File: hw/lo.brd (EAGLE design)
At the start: 23.8 x 33 mm, 40 parts, among them U1 ADF4360-9, X1 CLK, X2 DATA, X3 LE, X4 DIVOUT, X7 VIN

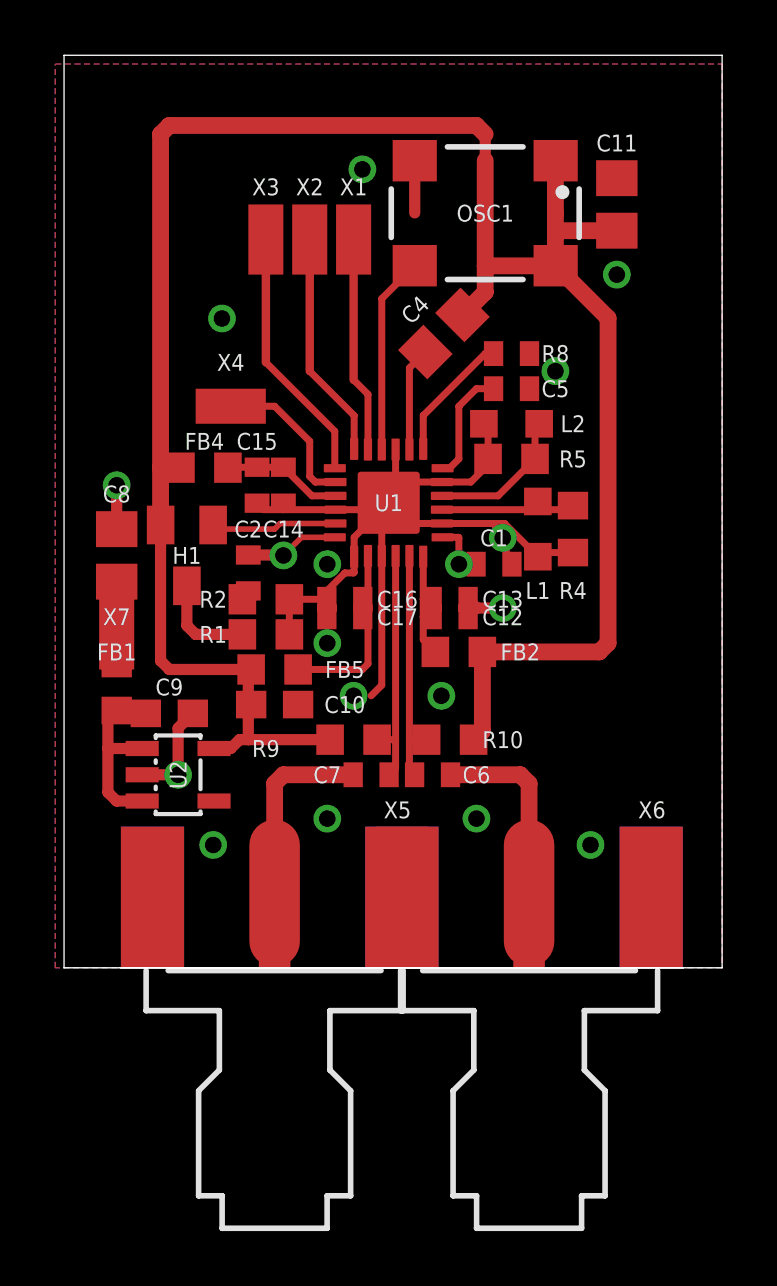
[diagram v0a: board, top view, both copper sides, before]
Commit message: optimize layout for easier soldering
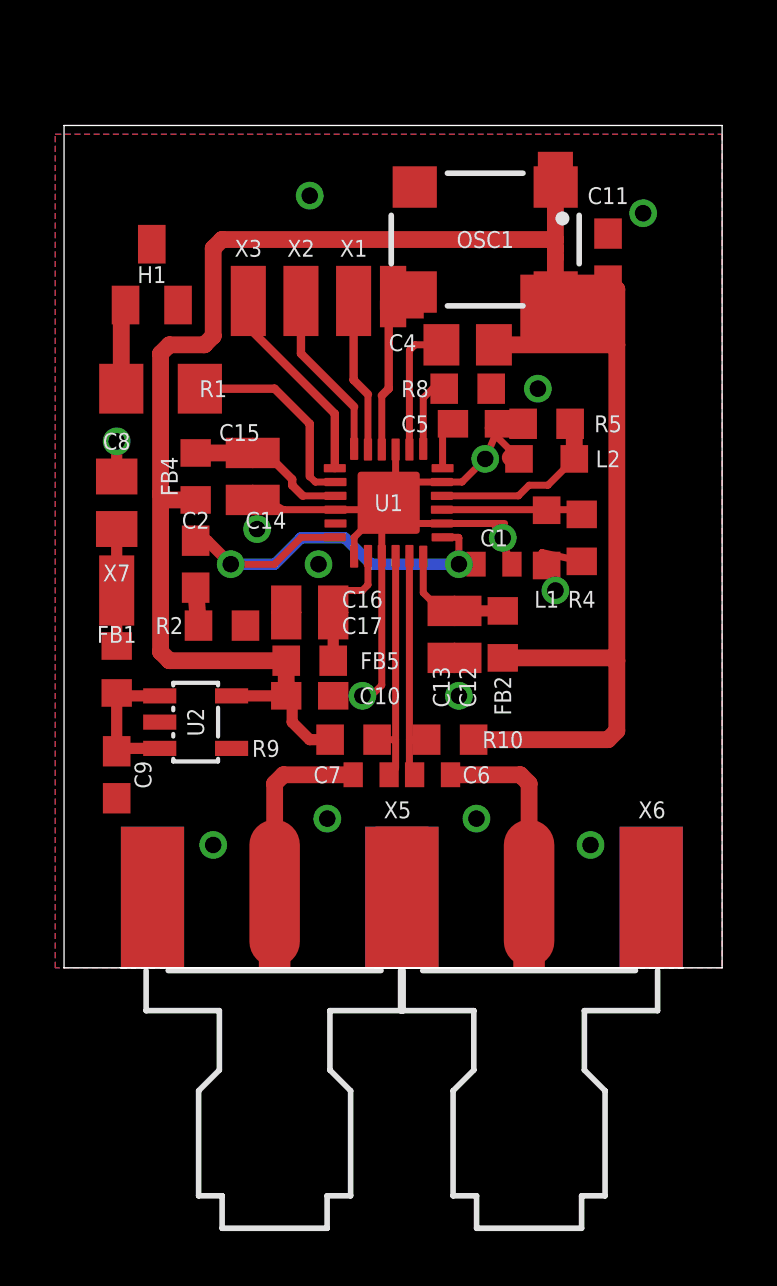
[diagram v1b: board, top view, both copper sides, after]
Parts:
- removed X4: DIVOUT, wirepad:SMD1,27-2,54
- C11: device rcl:C0805 -> rcl:C0603
- C12, C13, C14, C15, C16, C17, C2, C5: device rcl:C0402 -> rcl:C0603
- R1: device rcl:R0603 -> rcl:R1206
- R8: device rcl:R0402 -> rcl:R0603
- moved H1 10.2 mm to (3.17, 25.1), turned to 0 degrees
- moved R1 9.67 mm to (3.49, 21.0), turned to 180 degrees
- moved C9 2.93 mm to (1.91, 6.99), turned to 270 degrees
- moved X3 2.31 mm to (6.67, 24.1)
- moved X2 2.25 mm to (8.57, 24.1)
- moved X1 2.22 mm to (10.5, 24.1)
- moved R8 2.03 mm to (14.6, 21.0)
- moved U2 2.01 mm to (4.76, 8.89)
- moved C2 1.93 mm to (4.76, 14.6)
- moved C11 1.93 mm to (19.7, 25.7)
- moved C8 1.91 mm to (1.91, 16.8)
- moved R2 1.85 mm to (5.71, 12.4)
- moved C5 1.80 mm to (14.9, 19.7)
- moved L2 1.80 mm to (17.5, 18.4)
- moved R5 1.80 mm to (17.5, 19.7)
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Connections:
- removed net N$8: U1.20, X4.1
- net GND: now also H1.3; no longer R1.2
- net N$5: now also R1.1, U1.20; no longer H1.1, U1.23
- net N$6: now also H1.1, R1.2; no longer H1.3, R1.1
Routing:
- net LD: track 5.58 -> 17.0 mm
- net GND: track 44.8 -> 33.6 mm, vias 16 -> 15
- net N$8: track 5.67 -> 0.00 mm
- net N$5: track 4.57 -> 7.42 mm
- net +3V3: track 83.3 -> 80.7 mm
- net N$15: track 4.15 -> 1.80 mm
- net N$35: track 7.02 -> 4.74 mm
- net N$1: track 7.82 -> 5.59 mm
- net N$2: track 8.24 -> 6.15 mm
- net N$3: track 9.31 -> 7.35 mm
- net N$29: track 4.68 -> 2.74 mm
- net N$33: track 4.33 -> 5.83 mm
- net N$4: track 6.80 -> 5.31 mm
- net N$13: track 5.26 -> 6.74 mm
- net N$16: track 2.96 -> 4.23 mm
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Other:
- board size 23.8 x 33 mm -> 23.8 x 30.5 mm
- board text added: "CLK"
- board text added: "DATA"
- board text added: "LE"
